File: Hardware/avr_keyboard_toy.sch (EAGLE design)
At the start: 20 parts, among them IC1 7805T, IC2 MCP23017SP, U1 ATMEGA328P-PU

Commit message: Hooked up TFT, SD and MCP to enable pins, so eventually the software can put the whole device to sleep.  Brought out the remaining 4 MCU pins to a MISC header.
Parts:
- added MISC: (no value), SparkFun-Connectors:M04PTH
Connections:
- new net AREF: MISC.1, U1.AREF
- new net MCP_EN: IC2.VSS, U1.PC2
- new net PC3: MISC.4, U1.PC3
- new net PD2: MISC.2, U1.PD2
- new net PD6: MISC.3, U1.PD6
- new net SD_EN: TFT-13.S, U1.PC1
- new net TFT_EN: TFT-1.S, U1.PC0
- net GND: no longer IC2.VSS, TFT-1.S, TFT-13.S
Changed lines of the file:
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@@
 <part name="GND2" library="supply1" deviceset="GND" device=""/>
 <part name="GND3" library="supply1" deviceset="GND" device=""/>
-<part name="GND4" library="supply1" deviceset="GND" device=""/>
 <part name="GND5" library="supply1" deviceset="GND" device=""/>
 <part name="P+1" library="supply1" deviceset="+5V" device=""/>
@@
 <part name="GND10" library="supply1" deviceset="GND" device=""/>
 <part name="GND11" library="supply1" deviceset="GND" device=""/>
-<part name="GND12" library="supply1" deviceset="GND" device=""/>
 <part name="GND13" library="supply1" deviceset="GND" device=""/>
 <part name="GND14" library="supply1" deviceset="GND" device=""/>
 <part name="GND15" library="supply1" deviceset="GND" device=""/>
 <part name="P+11" library="supply1" deviceset="VCC" device=""/>
+<part name="MISC" library="SparkFun-Connectors" deviceset="M04" device="PTH"/>
 </parts>
 <sheets>
@@
 <instance part="J5" gate="A" x="68.58" y="22.86" rot="R90"/>
 <instance part="GND1" gate="1" x="58.42" y="7.62"/>
-<instance part="GND2" gate="1" x="7.62" y="-5.08"/>
+<instance part="GND2" gate="1" x="0" y="-5.08"/>
 <instance part="GND3" gate="1" x="30.48" y="71.12"/>
-<instance part="GND4" gate="1" x="193.04" y="78.74"/>
 <instance part="GND5" gate="1" x="147.32" y="170.18"/>
 <instance part="P+1" gate="1" x="147.32" y="190.5"/>
@@
 <instance part="GND10" gate="1" x="119.38" y="139.7"/>
 <instance part="GND11" gate="1" x="78.74" y="139.7"/>
-<instance part="GND12" gate="1" x="187.96" y="116.84"/>
 <instance part="GND13" gate="1" x="129.54" y="71.12"/>
 <instance part="GND14" gate="1" x="109.22" y="83.82"/>
 <instance part="GND15" gate="1" x="149.86" y="86.36"/>
 <instance part="P+11" gate="VCC" x="93.98" y="93.98"/>
+<instance part="MISC" gate="G$1" x="154.94" y="147.32"/>
 </instances>
 <busses>
@@
 <net name="GND" class="0">
 <segment>
-<pinref part="GND2" gate="1" pin="GND"/>
-<wire x1="7.62" y1="-2.54" x2="7.62" y2="2.54" width="0.1524" layer="91"/>
-<pinref part="IC2" gate="G$1" pin="VSS"/>
-<wire x1="7.62" y1="2.54" x2="15.24" y2="2.54" width="0.1524" layer="91"/>
-<wire x1="7.62" y1="2.54" x2="7.62" y2="7.62" width="0.1524" layer="91"/>
-<junction x="7.62" y="2.54"/>
-<pinref part="IC2" gate="G$1" pin="A0"/>
-<wire x1="7.62" y1="7.62" x2="7.62" y2="10.16" width="0.1524" layer="91"/>
-<wire x1="7.62" y1="10.16" x2="7.62" y2="12.7" width="0.1524" layer="91"/>
-<wire x1="7.62" y1="12.7" x2="15.24" y2="12.7" width="0.1524" layer="91"/>
-<pinref part="IC2" gate="G$1" pin="A1"/>
-<wire x1="7.62" y1="10.16" x2="15.24" y2="10.16" width="0.1524" layer="91"/>
-<junction x="7.62" y="10.16"/>
-<pinref part="IC2" gate="G$1" pin="A2"/>
-<wire x1="7.62" y1="7.62" x2="15.24" y2="7.62" width="0.1524" layer="91"/>
-<junction x="7.62" y="7.62"/>
-</segment>
-<segment>
 <pinref part="J5" gate="A" pin="1"/>
 <pinref part="GND1" gate="1" pin="GND"/>
@@
 <wire x1="30.48" y1="78.74" x2="40.64" y2="78.74" width="0.1524" layer="91"/>
 <junction x="30.48" y="78.74"/>
-</segment>
-<segment>
-<pinref part="GND4" gate="1" pin="GND"/>
-<wire x1="193.04" y1="81.28" x2="193.04" y2="83.82" width="0.1524" layer="91"/>
-<pinref part="TFT" gate="-13" pin="S"/>
-<wire x1="193.04" y1="83.82" x2="213.36" y2="83.82" width="0.1524" layer="91"/>
 </segment>
 <segment>
@@
 </segment>
 <segment>
-<pinref part="GND12" gate="1" pin="GND"/>
-<wire x1="187.96" y1="119.38" x2="187.96" y2="121.92" width="0.1524" layer="91"/>
-<wire x1="187.96" y1="121.92" x2="198.12" y2="121.92" width="0.1524" layer="91"/>
-<wire x1="198.12" y1="121.92" x2="198.12" y2="114.3" width="0.1524" layer="91"/>
-<pinref part="TFT" gate="-1" pin="S"/>
-<wire x1="198.12" y1="114.3" x2="213.36" y2="114.3" width="0.1524" layer="91"/>
-<label x="203.2" y="114.3" size="1.778" layer="95"/>
+<pinref part="IC2" gate="G$1" pin="A0"/>
+<wire x1="15.24" y1="12.7" x2="0" y2="12.7" width="0.1524" layer="91"/>
+<pinref part="GND2" gate="1" pin="GND"/>
+<wire x1="0" y1="12.7" x2="0" y2="10.16" width="0.1524" layer="91"/>
+<pinref part="IC2" gate="G$1" pin="A1"/>
+<wire x1="0" y1="10.16" x2="0" y2="7.62" width="0.1524" layer="91"/>
+<wire x1="0" y1="7.62" x2="0" y2="-2.54" width="0.1524" layer="91"/>
+<wire x1="15.24" y1="10.16" x2="0" y2="10.16" width="0.1524" layer="91"/>
+<junction x="0" y="10.16"/>
+<pinref part="IC2" gate="G$1" pin="A2"/>
+<wire x1="0" y1="7.62" x2="15.24" y2="7.62" width="0.1524" layer="91"/>
+<junction x="0" y="7.62"/>
 </segment>
 </net>
@@
 </segment>
 </net>
+<net name="TFT_EN" class="0">
+<segment>
+<pinref part="U1" gate="A" pin="PC0"/>
+<wire x1="83.82" y1="93.98" x2="76.2" y2="93.98" width="0.1524" layer="91"/>
+<label x="78.74" y="93.98" size="1.778" layer="95"/>
+</segment>
+<segment>
+<pinref part="TFT" gate="-1" pin="S"/>
+<wire x1="203.2" y1="114.3" x2="213.36" y2="114.3" width="0.1524" layer="91"/>
+<label x="203.2" y="114.3" size="1.778" layer="95"/>
+</segment>
+</net>
+<net name="SD_EN" class="0">
+<segment>
+<pinref part="U1" gate="A" pin="PC1"/>
+<wire x1="83.82" y1="91.44" x2="76.2" y2="91.44" width="0.1524" layer="91"/>
+<label x="78.74" y="91.44" size="1.778" layer="95"/>
+</segment>
+<segment>
+<pinref part="TFT" gate="-13" pin="S"/>
+<wire x1="203.2" y1="83.82" x2="213.36" y2="83.82" width="0.1524" layer="91"/>
+<label x="203.2" y="83.82" size="1.778" layer="95"/>
+</segment>
+</net>
+<net name="MCP_EN" class="0">
+<segment>
+<pinref part="U1" gate="A" pin="PC2"/>
+<wire x1="83.82" y1="88.9" x2="76.2" y2="88.9" width="0.1524" layer="91"/>
+<label x="78.74" y="88.9" size="1.778" layer="95"/>
+</segment>
+<segment>
+<pinref part="IC2" gate="G$1" pin="VSS"/>
+<wire x1="7.62" y1="2.54" x2="15.24" y2="2.54" width="0.1524" layer="91"/>
+<label x="2.54" y="2.54" size="1.778" layer="95"/>
+</segment>
+</net>
+<net name="AREF" class="0">
+<segment>
+<pinref part="U1" gate="A" pin="AREF"/>
+<wire x1="33.02" y1="109.22" x2="40.64" y2="109.22" width="0.1524" layer="91"/>
+<label x="33.02" y="109.22" size="1.778" layer="95"/>
+</segment>
+<segment>
+<pinref part="MISC" gate="G$1" pin="1"/>
+<wire x1="167.64" y1="144.78" x2="160.02" y2="144.78" width="0.1524" layer="91"/>
+<label x="162.56" y="144.78" size="1.778" layer="95"/>
+</segment>
+</net>
+<net name="PD2" class="0">
+<segment>
+<pinref part="U1" gate="A" pin="PD2"/>
+<wire x1="83.82" y1="111.76" x2="76.2" y2="111.76" width="0.1524" layer="91"/>
+<label x="81.28" y="111.76" size="1.778" layer="95"/>
+</segment>
+<segment>
+<pinref part="MISC" gate="G$1" pin="2"/>
+<wire x1="167.64" y1="147.32" x2="160.02" y2="147.32" width="0.1524" layer="91"/>
+<label x="162.56" y="147.32" size="1.778" layer="95"/>
+</segment>
+</net>
+<net name="PD6" class="0">
+<segment>
+<pinref part="U1" gate="A" pin="PD6"/>
+<wire x1="83.82" y1="101.6" x2="76.2" y2="101.6" width="0.1524" layer="91"/>
+<label x="81.28" y="101.6" size="1.778" layer="95"/>
+</segment>
+<segment>
+<pinref part="MISC" gate="G$1" pin="3"/>
+<wire x1="167.64" y1="149.86" x2="160.02" y2="149.86" width="0.1524" layer="91"/>
+<label x="162.56" y="149.86" size="1.778" layer="95"/>
+</segment>
+</net>
+<net name="PC3" class="0">
+<segment>
+<pinref part="U1" gate="A" pin="PC3"/>
+<wire x1="83.82" y1="86.36" x2="76.2" y2="86.36" width="0.1524" layer="91"/>
+<label x="78.74" y="86.36" size="1.778" layer="95"/>
+</segment>
+<segment>
+<pinref part="MISC" gate="G$1" pin="4"/>
+<wire x1="167.64" y1="152.4" x2="160.02" y2="152.4" width="0.1524" layer="91"/>
+<label x="162.56" y="152.4" size="1.778" layer="95"/>
+</segment>
+</net>

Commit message: Progress on pcb
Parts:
- removed U$1: 2.1MMJACKTHM, adafruit:2.1MMJACKTHM
- renumbered J5 to GPIO
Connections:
- net +3V3: no longer U$1.TIP
- net GND: no longer U$1.RING, U$1.RING_SW
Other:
- note added: "A"
- note added: "AVR Keyboard Toy -- Tiny Basic Plus learning toy (c) 2016 Peter Dunshee http://petezah.com"

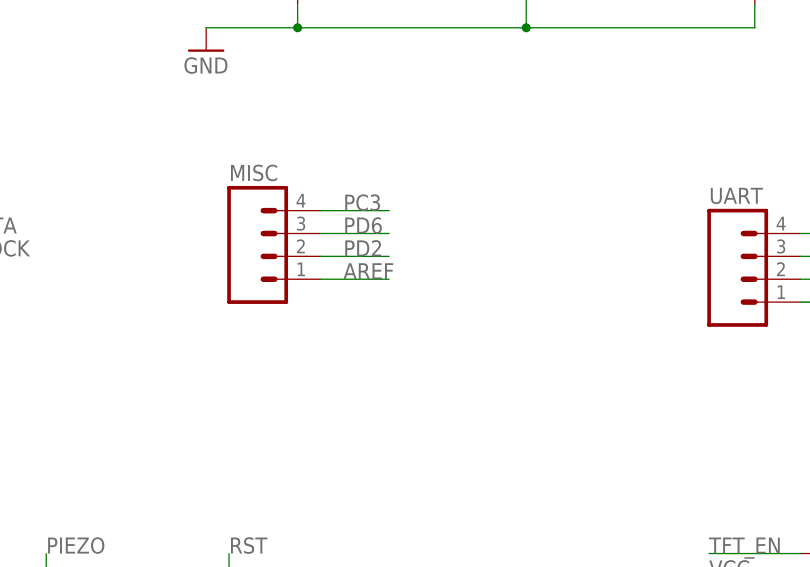
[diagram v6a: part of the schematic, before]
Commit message: Finished routing signals
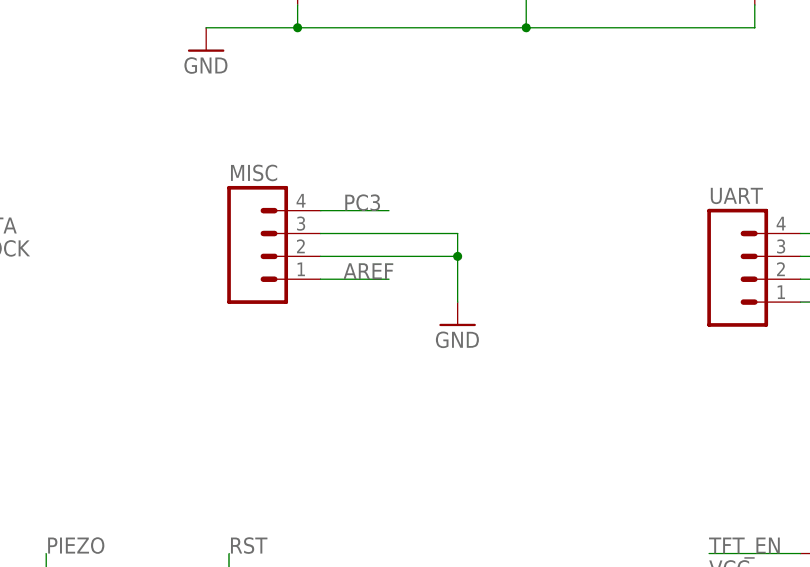
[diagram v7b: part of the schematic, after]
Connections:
- net GND: now also MISC.2, MISC.3
- net PD2: no longer MISC.2
- net PD6: no longer MISC.3
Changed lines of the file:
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@@
 <grid distance="0.1" unitdist="inch" unit="inch" style="lines" multiple="1" display="no" altdistance="0.01" altunitdist="inch" altunit="inch"/>
 <layers>
-<layer number="1" name="Top" color="4" fill="1" visible="yes" active="no"/>
-<layer number="16" name="Bottom" color="1" fill="1" visible="yes" active="no"/>
-<layer number="17" name="Pads" color="2" fill="1" visible="yes" active="no"/>
-<layer number="18" name="Vias" color="2" fill="1" visible="yes" active="no"/>
-<layer number="19" name="Unrouted" color="6" fill="1" visible="yes" active="no"/>
-<layer number="20" name="Dimension" color="15" fill="1" visible="yes" active="no"/>
-<layer number="21" name="tPlace" color="7" fill="1" visible="yes" active="no"/>
-<layer number="22" name="bPlace" color="7" fill="1" visible="yes" active="no"/>
-<layer number="23" name="tOrigins" color="15" fill="1" visible="yes" active="no"/>
-<layer number="24" name="bOrigins" color="15" fill="1" visible="yes" active="no"/>
-<layer number="25" name="tNames" color="7" fill="1" visible="yes" active="no"/>
-<layer number="26" name="bNames" color="7" fill="1" visible="yes" active="no"/>
-<layer number="27" name="tValues" color="7" fill="1" visible="yes" active="no"/>
-<layer number="28" name="bValues" color="7" fill="1" visible="yes" active="no"/>
+<layer number="1" name="Top" color="4" fill="1" visible="no" active="no"/>
+<layer number="16" name="Bottom" color="1" fill="1" visible="no" active="no"/>
+<layer number="17" name="Pads" color="2" fill="1" visible="no" active="no"/>
+<layer number="18" name="Vias" color="2" fill="1" visible="no" active="no"/>
+<layer number="19" name="Unrouted" color="6" fill="1" visible="no" active="no"/>
+<layer number="20" name="Dimension" color="15" fill="1" visible="no" active="no"/>
+<layer number="21" name="tPlace" color="7" fill="1" visible="no" active="no"/>
+<layer number="22" name="bPlace" color="7" fill="1" visible="no" active="no"/>
+<layer number="23" name="tOrigins" color="15" fill="1" visible="no" active="no"/>
+<layer number="24" name="bOrigins" color="15" fill="1" visible="no" active="no"/>
+<layer number="25" name="tNames" color="7" fill="1" visible="no" active="no"/>
+<layer number="26" name="bNames" color="7" fill="1" visible="no" active="no"/>
+<layer number="27" name="tValues" color="7" fill="1" visible="no" active="no"/>
+<layer number="28" name="bValues" color="7" fill="1" visible="no" active="no"/>
 <layer number="29" name="tStop" color="7" fill="3" visible="no" active="no"/>
 <layer number="30" name="bStop" color="7" fill="6" visible="no" active="no"/>
@@
 <layer number="35" name="tGlue" color="7" fill="4" visible="no" active="no"/>
 <layer number="36" name="bGlue" color="7" fill="5" visible="no" active="no"/>
-<layer number="37" name="tTest" color="7" fill="1" visible="yes" active="no"/>
-<layer number="38" name="bTest" color="7" fill="1" visible="yes" active="no"/>
+<layer number="37" name="tTest" color="7" fill="1" visible="no" active="no"/>
+<layer number="38" name="bTest" color="7" fill="1" visible="no" active="no"/>
 <layer number="39" name="tKeepout" color="4" fill="11" visible="no" active="no"/>
 <layer number="40" name="bKeepout" color="1" fill="11" visible="no" active="no"/>
@@
 <layer number="44" name="Drills" color="7" fill="1" visible="no" active="no"/>
 <layer number="45" name="Holes" color="7" fill="1" visible="no" active="no"/>
-<layer number="46" name="Milling" color="3" fill="1" visible="yes" active="no"/>
-<layer number="47" name="Measures" color="7" fill="1" visible="yes" active="no"/>
-<layer number="48" name="Document" color="7" fill="1" visible="yes" active="no"/>
-<layer number="49" name="Reference" color="7" fill="1" visible="yes" active="no"/>
-<layer number="50" name="dxf" color="7" fill="1" visible="yes" active="no"/>
-<layer number="51" name="tDocu" color="7" fill="1" visible="yes" active="no"/>
-<layer number="52" name="bDocu" color="7" fill="1" visible="yes" active="no"/>
-<layer number="53" name="tGND_GNDA" color="7" fill="9" visible="yes" active="no"/>
-<layer number="54" name="bGND_GNDA" color="1" fill="9" visible="yes" active="no"/>
-<layer number="56" name="wert" color="7" fill="1" visible="yes" active="no"/>
-<layer number="57" name="tCAD" color="7" fill="1" visible="yes" active="no"/>
-<layer number="59" name="tCarbon" color="7" fill="1" visible="yes" active="no"/>
-<layer number="60" name="bCarbon" color="7" fill="1" visible="yes" active="no"/>
+<layer number="46" name="Milling" color="3" fill="1" visible="no" active="no"/>
+<layer number="47" name="Measures" color="7" fill="1" visible="no" active="no"/>
+<layer number="48" name="Document" color="7" fill="1" visible="no" active="no"/>
+<layer number="49" name="Reference" color="7" fill="1" visible="no" active="no"/>
+<layer number="50" name="dxf" color="7" fill="1" visible="no" active="no"/>
+<layer number="51" name="tDocu" color="7" fill="1" visible="no" active="no"/>
+<layer number="52" name="bDocu" color="7" fill="1" visible="no" active="no"/>
+<layer number="53" name="tGND_GNDA" color="7" fill="9" visible="no" active="no"/>
+<layer number="54" name="bGND_GNDA" color="1" fill="9" visible="no" active="no"/>
+<layer number="56" name="wert" color="7" fill="1" visible="no" active="no"/>
+<layer number="57" name="tCAD" color="7" fill="1" visible="no" active="no"/>
+<layer number="59" name="tCarbon" color="7" fill="1" visible="no" active="no"/>
+<layer number="60" name="bCarbon" color="7" fill="1" visible="no" active="no"/>
 <layer number="90" name="Modules" color="5" fill="1" visible="yes" active="yes"/>
 <layer number="91" name="Nets" color="2" fill="1" visible="yes" active="yes"/>
@@
 <part name="P+11" library="supply1" deviceset="VCC" device=""/>
 <part name="MISC" library="SparkFun-Connectors" deviceset="M04" device="PTH"/>
+<part name="GND4" library="supply1" deviceset="GND" device=""/>
 </parts>
 <sheets>
@@
 <instance part="P+11" gate="VCC" x="93.98" y="93.98"/>
 <instance part="MISC" gate="G$1" x="154.94" y="147.32"/>
+<instance part="GND4" gate="1" x="175.26" y="139.7"/>
 </instances>
 <busses>
@@
 <junction x="0" y="7.62"/>
 </segment>
+<segment>
+<pinref part="GND4" gate="1" pin="GND"/>
+<wire x1="175.26" y1="142.24" x2="175.26" y2="147.32" width="0.1524" layer="91"/>
+<pinref part="MISC" gate="G$1" pin="2"/>
+<wire x1="175.26" y1="147.32" x2="160.02" y2="147.32" width="0.1524" layer="91"/>
+<pinref part="MISC" gate="G$1" pin="3"/>
+<wire x1="160.02" y1="149.86" x2="175.26" y2="149.86" width="0.1524" layer="91"/>
+<wire x1="175.26" y1="149.86" x2="175.26" y2="147.32" width="0.1524" layer="91"/>
+<junction x="175.26" y="147.32"/>
+</segment>
 </net>
 <net name="SS" class="0">
@@
 <label x="81.28" y="111.76" size="1.778" layer="95"/>
 </segment>
-<segment>
-<pinref part="MISC" gate="G$1" pin="2"/>
-<wire x1="167.64" y1="147.32" x2="160.02" y2="147.32" width="0.1524" layer="91"/>
-<label x="162.56" y="147.32" size="1.778" layer="95"/>
-</segment>
 </net>
 <net name="PD6" class="0">
@@
 <label x="81.28" y="101.6" size="1.778" layer="95"/>
 </segment>
-<segment>
-<pinref part="MISC" gate="G$1" pin="3"/>
-<wire x1="167.64" y1="149.86" x2="160.02" y2="149.86" width="0.1524" layer="91"/>
-<label x="162.56" y="149.86" size="1.778" layer="95"/>
-</segment>
-</net>
+</net>
